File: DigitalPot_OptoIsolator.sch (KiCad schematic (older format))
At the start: 18 parts, among them J1 DIN-5, J2 5-Way Pin Header, U1 TLP2361, U2 TLP2361, U3 TLP2361, U4 FODM8801

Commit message: Tidied up the schematics
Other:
- note added: "DIGITAL\nPOTENTIOMETER"
- note added: "MCP CONTROL UNIT"
- moved on the sheet: C1, C2, C3, C4, H1, H2, H3, H4, J1, J2

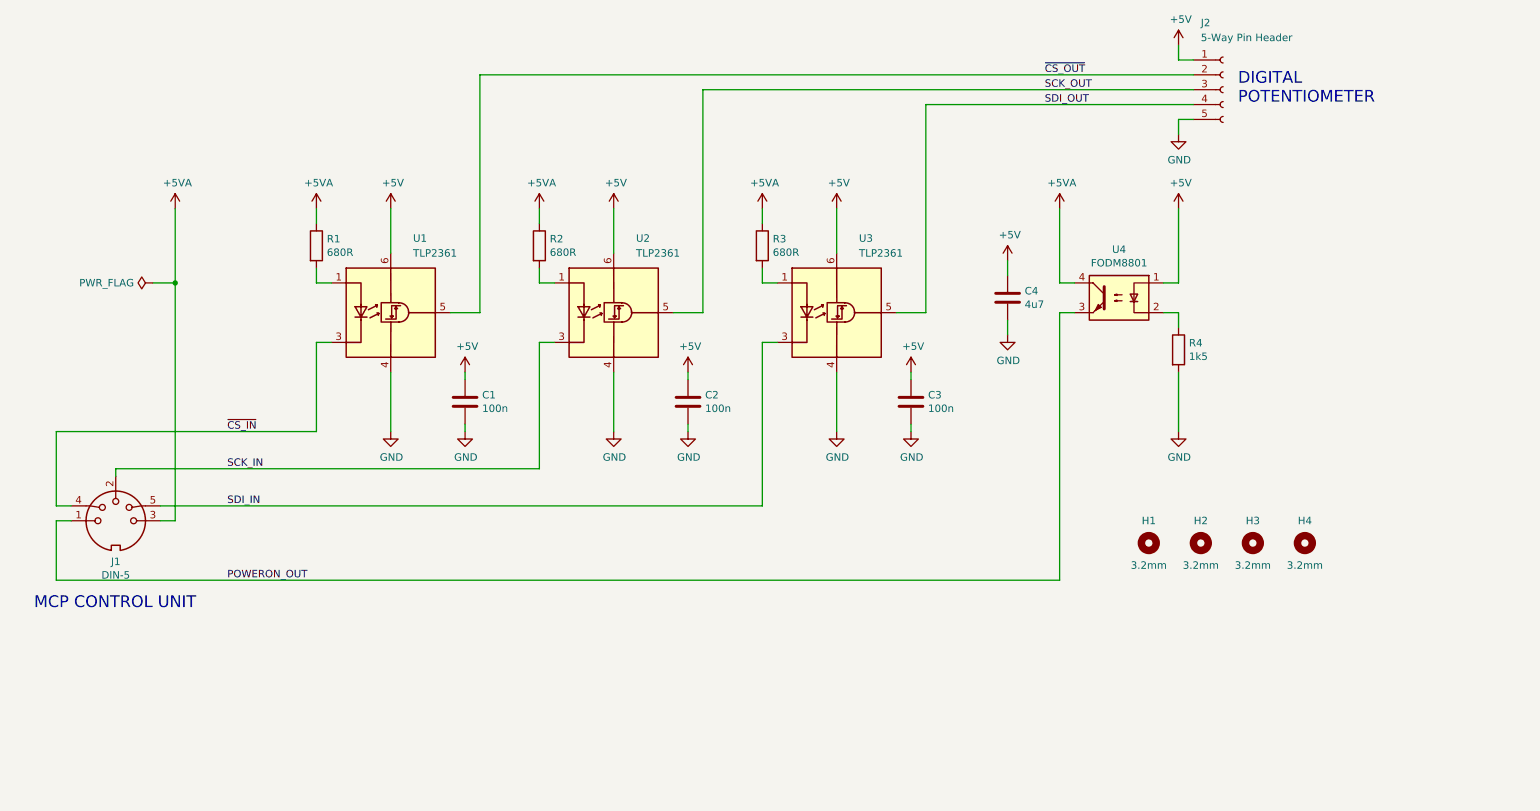
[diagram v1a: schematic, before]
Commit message: Added the aluminium enclosure to the schematics
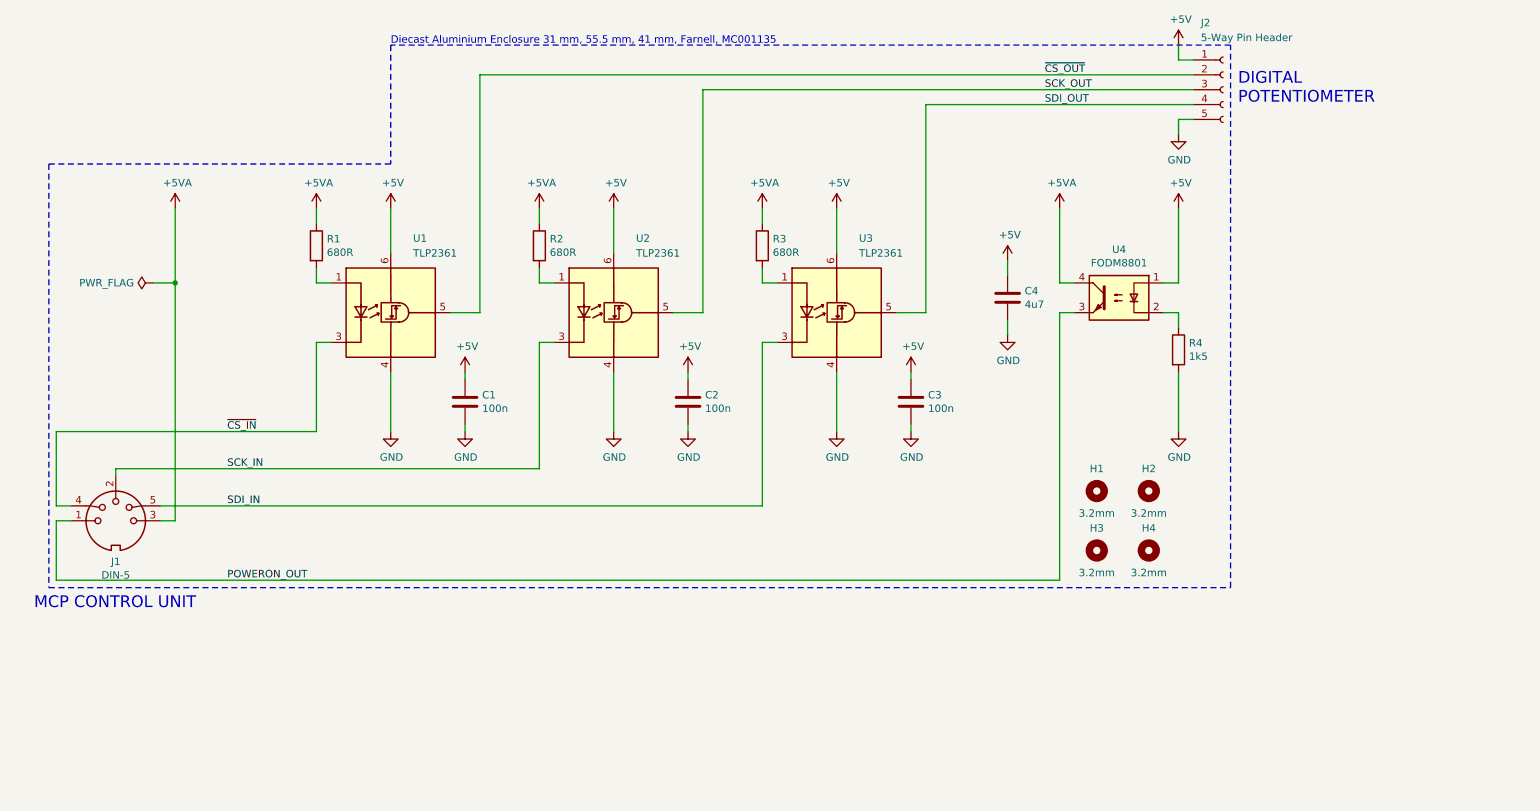
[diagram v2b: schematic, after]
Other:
- note added: "Diecast Aluminium Enclosure 31 mm, 55.5 mm, 41 mm, Farnell, MC001135"
- moved on the sheet: H1, H2, H3, H4
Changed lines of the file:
@@
 L Mechanical:MountingHole H1
 U 1 1 5D372A24
-P 8600 4250
-F 0 "H1" H 8600 4400 50  0000 C CNN
-F 1 "3.2mm" H 8600 4100 50  0000 C CNN
-F 2 "MountingHole:MountingHole_3.2mm_M3" H 8600 4250 50  0001 C CNN
-F 3 "~" H 8600 4250 50  0001 C CNN
-	1    8600 4250
+P 8250 3900
+F 0 "H1" H 8250 4050 50  0000 C CNN
+F 1 "3.2mm" H 8250 3750 50  0000 C CNN
+F 2 "MountingHole:MountingHole_3.2mm_M3" H 8250 3900 50  0001 C CNN
+F 3 "~" H 8250 3900 50  0001 C CNN
+	1    8250 3900
 	1    0    0    -1
 $EndComp
@@
 L Mechanical:MountingHole H2
 U 1 1 5D3741F9
-P 8950 4250
-F 0 "H2" H 8950 4400 50  0000 C CNN
-F 1 "3.2mm" H 8950 4100 50  0000 C CNN
-F 2 "MountingHole:MountingHole_3.2mm_M3" H 8950 4250 50  0001 C CNN
-F 3 "~" H 8950 4250 50  0001 C CNN
-	1    8950 4250
+P 8600 3900
+F 0 "H2" H 8600 4050 50  0000 C CNN
+F 1 "3.2mm" H 8600 3750 50  0000 C CNN
+F 2 "MountingHole:MountingHole_3.2mm_M3" H 8600 3900 50  0001 C CNN
+F 3 "~" H 8600 3900 50  0001 C CNN
+	1    8600 3900
 	1    0    0    -1
 $EndComp
@@
 L Mechanical:MountingHole H3
 U 1 1 5D374824
-P 9300 4250
-F 0 "H3" H 9300 4400 50  0000 C CNN
-F 1 "3.2mm" H 9300 4100 50  0000 C CNN
-F 2 "MountingHole:MountingHole_3.2mm_M3" H 9300 4250 50  0001 C CNN
-F 3 "~" H 9300 4250 50  0001 C CNN
-	1    9300 4250
+P 8250 4300
+F 0 "H3" H 8250 4450 50  0000 C CNN
+F 1 "3.2mm" H 8250 4150 50  0000 C CNN
+F 2 "MountingHole:MountingHole_3.2mm_M3" H 8250 4300 50  0001 C CNN
+F 3 "~" H 8250 4300 50  0001 C CNN
+	1    8250 4300
 	1    0    0    -1
 $EndComp
@@
 L Mechanical:MountingHole H4
 U 1 1 5D374AEC
-P 9650 4250
-F 0 "H4" H 9650 4400 50  0000 C CNN
-F 1 "3.2mm" H 9650 4100 50  0000 C CNN
-F 2 "MountingHole:MountingHole_3.2mm_M3" H 9650 4250 50  0001 C CNN
-F 3 "~" H 9650 4250 50  0001 C CNN
-	1    9650 4250
+P 8600 4300
+F 0 "H4" H 8600 4450 50  0000 C CNN
+F 1 "3.2mm" H 8600 4150 50  0000 C CNN
+F 2 "MountingHole:MountingHole_3.2mm_M3" H 8600 4300 50  0001 C CNN
+F 3 "~" H 8600 4300 50  0001 C CNN
+	1    8600 4300
 	1    0    0    -1
 $EndComp
@@
 Text Notes 1100 4700 0    79   ~ 0
 MCP CONTROL UNIT
+Wire Notes Line
+	1200 4550 9150 4550
+Wire Notes Line
+	9150 4550 9150 900
+Wire Notes Line
+	9150 900  3500 900
+Wire Notes Line
+	1200 1700 1200 4550
+Text Notes 3500 900  0    50   ~ 0
+Diecast Aluminium Enclosure 31 mm, 55.5 mm, 41 mm, Farnell, MC001135
+Wire Notes Line
+	3500 900  3500 1700
+Wire Notes Line
+	3500 1700 1200 1700
 $EndSCHEMATC
